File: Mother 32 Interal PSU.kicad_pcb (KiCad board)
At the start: 2 copper layers, 200.7 x 40.6 mm, 24 parts, among them P1 CONN_01X02, P2 CONN_02X08, P3 CONN_02X08, P4 CONN_02X08, P5 CONN_02X08, P6 CONN_02X08, P7 CONN_02X08, P8 CONN_02X08, P9 CONN_02X08, U1 BPM15, U2 R-78E5.0-0.5

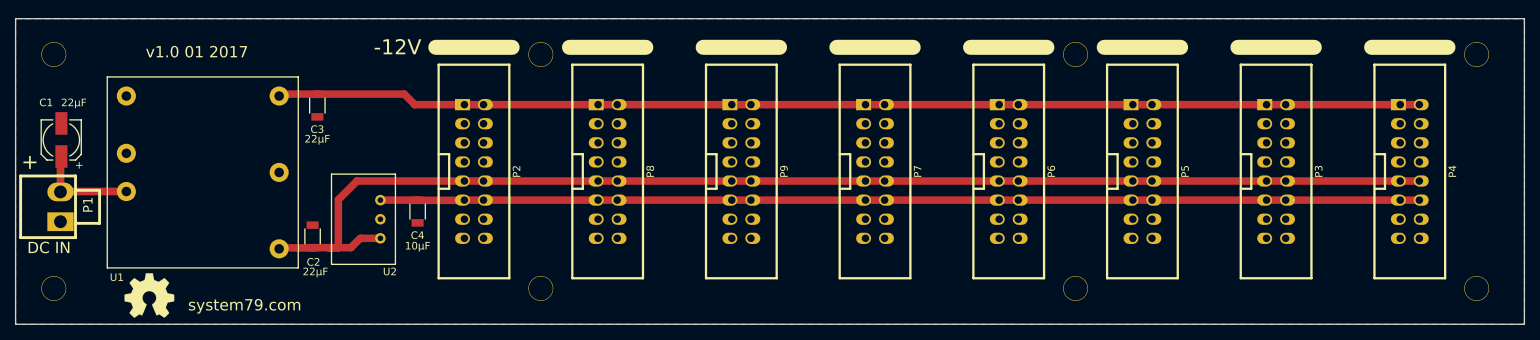
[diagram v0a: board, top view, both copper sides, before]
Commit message: updated silkscreen
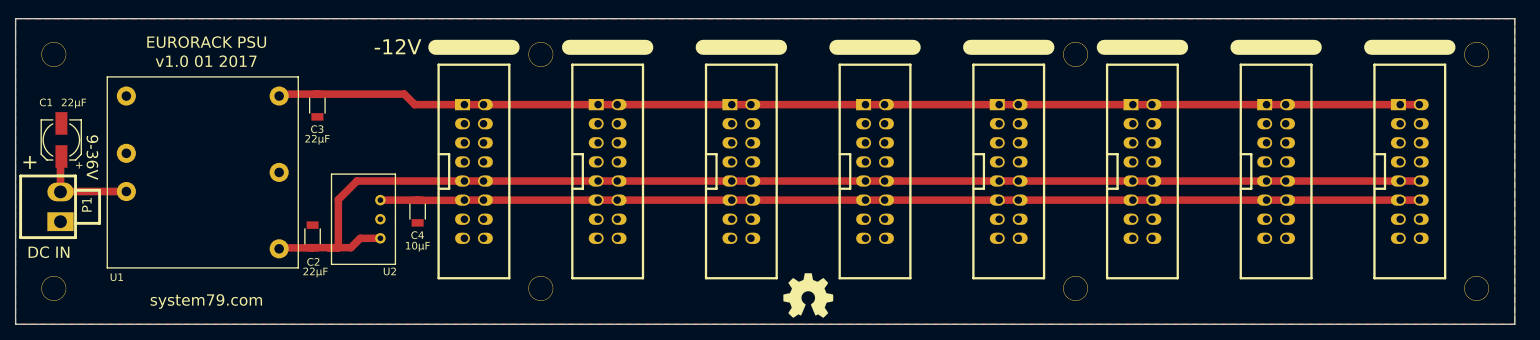
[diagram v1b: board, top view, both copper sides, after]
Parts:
- moved REF*** 87.6 mm to (143.5, 113.0)
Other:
- board size 200.7 x 40.6 mm -> 199.4 x 40.6 mm
- board text added: "9-36V"
- board text added: "EURORACK PSU"
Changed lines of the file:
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@@
     (links 109)
     (no_connects 0)
-    (area 38.024999 76.124999 238.835001 116.915001)
+    (area 38.024999 76.124999 237.565001 116.915001)
     (thickness 1.6)
-    (drawings 17)
+    (drawings 19)
     (tracks 72)
     (zones 0)
@@
     (descr "Box header 8x2pin 2.54mm")
     (tags "CONN DEV")
-    (fp_text reference P9 (at 0 -5.7 270) (layer F.SilkS)
+    (fp_text reference P9 (at 0 -5.7 270) (layer F.SilkS) hide
       (effects (font (size 1 1) (thickness 0.2032)))
     )
@@
     (descr "Box header 8x2pin 2.54mm")
     (tags "CONN DEV")
-    (fp_text reference P8 (at 0 -5.7 270) (layer F.SilkS)
+    (fp_text reference P8 (at 0 -5.7 270) (layer F.SilkS) hide
       (effects (font (size 1 1) (thickness 0.2032)))
     )
@@
     (descr "Box header 8x2pin 2.54mm")
     (tags "CONN DEV")
-    (fp_text reference P7 (at 0 -5.7 270) (layer F.SilkS)
+    (fp_text reference P7 (at 0 -5.7 270) (layer F.SilkS) hide
       (effects (font (size 1 1) (thickness 0.2032)))
     )
@@
     (descr "Box header 8x2pin 2.54mm")
     (tags "CONN DEV")
-    (fp_text reference P6 (at 0 -5.7 270) (layer F.SilkS)
+    (fp_text reference P6 (at 0 -5.7 270) (layer F.SilkS) hide
       (effects (font (size 1 1) (thickness 0.2032)))
     )
@@
     (descr "Box header 8x2pin 2.54mm")
     (tags "CONN DEV")
-    (fp_text reference P5 (at 0 -5.7 270) (layer F.SilkS)
+    (fp_text reference P5 (at 0 -5.7 270) (layer F.SilkS) hide
       (effects (font (size 1 1) (thickness 0.2032)))
     )
@@
     (descr "Box header 8x2pin 2.54mm")
     (tags "CONN DEV")
-    (fp_text reference P4 (at 0 -5.7 270) (layer F.SilkS)
+    (fp_text reference P4 (at 0 -5.7 270) (layer F.SilkS) hide
       (effects (font (size 1 1) (thickness 0.2032)))
     )
@@
     (descr "Box header 8x2pin 2.54mm")
     (tags "CONN DEV")
-    (fp_text reference P3 (at 0 -5.7 270) (layer F.SilkS)
+    (fp_text reference P3 (at 0 -5.7 270) (layer F.SilkS) hide
       (effects (font (size 1 1) (thickness 0.2032)))
     )
@@
     (descr "Box header 8x2pin 2.54mm")
     (tags "CONN DEV")
-    (fp_text reference P2 (at 0 -5.7 270) (layer F.SilkS)
+    (fp_text reference P2 (at 0 -5.7 360) (layer F.SilkS) hide
       (effects (font (size 1 1) (thickness 0.2032)))
     )
@@
     (at 44.069 101.219 270)
     (descr "2 pin vert. connector, Molex KK156 series")
-    (fp_text reference P1 (at -0.254 -3.683 450) (layer F.SilkS)
+    (fp_text reference P1 (at -0.254 -3.556 450) (layer F.SilkS)
       (effects (font (thickness 0.3048)))
     )
@@
   )
   (module Symbols:OSHW-Symbol_6.7x6mm_SilkScreen (layer F.Cu)
-    (at 55.88 113.03)
+    (at 143.51 113.03)
     (descr "Open Source Hardware Symbol")
     (tags "Logo Symbol OSHW")
@@
       (xy 0.555814 -2.531069)) (layer F.SilkS) (width 0.01))
   )
-  (gr_text "v1.0 01 2017" (at 62.23 80.645) (layer F.SilkS)
+  (gr_text 9-36V (at 48.26 94.615 270) (layer F.SilkS)
     (effects (font (size 1.5 1.5) (thickness 0.3)))
   )
-  (gr_text system79.com (at 68.58 114.3) (layer F.SilkS)
+  (gr_text "EURORACK PSU" (at 63.5 79.375) (layer F.SilkS)
     (effects (font (size 1.5 1.5) (thickness 0.3)))
   )
-  (gr_text "DC IN" (at 42.545 106.68) (layer F.SilkS)
+  (gr_text "v1.0 01 2017" (at 63.5 81.915) (layer F.SilkS)
+    (effects (font (size 1.5 1.5) (thickness 0.3)))
+  )
+  (gr_text system79.com (at 63.5 113.665) (layer F.SilkS)
+    (effects (font (size 1.5 1.5) (thickness 0.3)))
+  )
+  (gr_text "DC IN" (at 42.545 107.315) (layer F.SilkS)
     (effects (font (size 1.5 1.5) (thickness 0.3)))
   )
@@
   (gr_line (start 93.98 80.01) (end 104.14 80.01) (angle 90) (layer F.SilkS) (width 2))
   (gr_line (start 38.1 116.84) (end 38.1 76.2) (layer Edge.Cuts) (width 0.15))
-  (gr_line (start 238.76 116.84) (end 38.1 116.84) (layer Edge.Cuts) (width 0.15))
-  (gr_line (start 238.76 76.2) (end 238.76 116.84) (angle 90) (layer Edge.Cuts) (width 0.15))
-  (gr_line (start 38.1 76.2) (end 238.76 76.2) (angle 90) (layer Edge.Cuts) (width 0.15))
+  (gr_line (start 237.49 116.84) (end 38.1 116.84) (layer Edge.Cuts) (width 0.15))
+  (gr_line (start 237.49 76.2) (end 237.49 116.84) (angle 90) (layer Edge.Cuts) (width 0.15))
+  (gr_line (start 38.1 76.2) (end 237.49 76.2) (angle 90) (layer Edge.Cuts) (width 0.15))
   (segment (start 44.069 99.239) (end 44.069 94.656) (width 1) (layer F.Cu) (net 1))
   (segment (start 44.069 94.656) (end 44.196 94.529) (width 1) (layer F.Cu) (net 1))
@@
     (polygon
       (pts
-        (xy 238.76 116.84) (xy 38.1 116.84) (xy 38.1 76.2) (xy 238.76 76.2) (xy 238.76 116.84)
+        (xy 237.49 116.84) (xy 38.1 116.84) (xy 38.1 76.2) (xy 237.49 76.2) (xy 237.49 116.84)
       )
     )

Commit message: updated ground planes and power traces, added CV/GATE connections
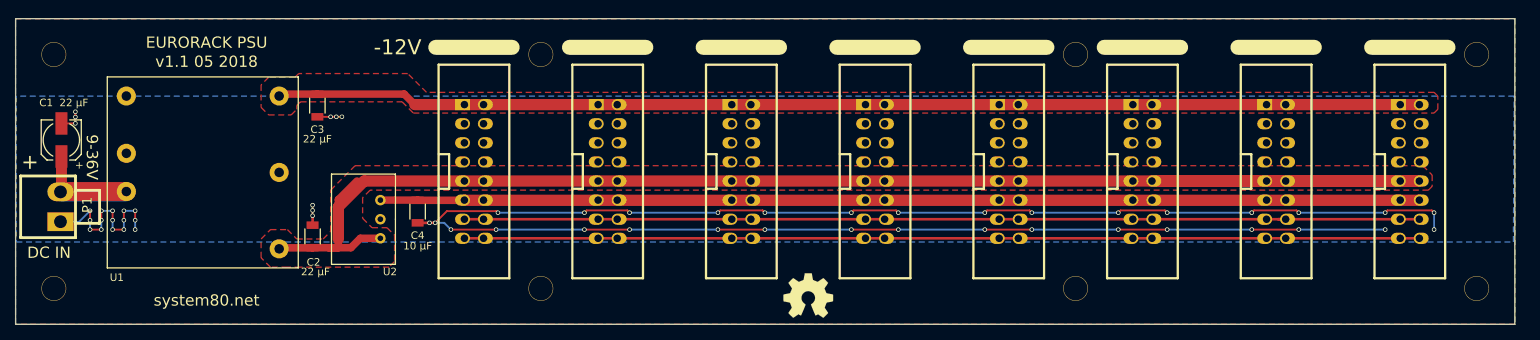
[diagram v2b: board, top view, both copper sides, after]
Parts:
- C1, C2, C3: value 22μF -> 22 μF
- C4: value 10μF -> 10 μF
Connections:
- P2 pad 13: Net-(P2-Pad13) -> /CV
- P2 pad 14: Net-(P2-Pad14) -> /CV
- P2 pad 15: Net-(P2-Pad15) -> /GATE
- P2 pad 16: Net-(P2-Pad16) -> /GATE
- P3 pad 13: Net-(P3-Pad13) -> /CV
- P3 pad 14: Net-(P3-Pad14) -> /CV
- P3 pad 15: Net-(P3-Pad15) -> /GATE
- P3 pad 16: Net-(P3-Pad16) -> /GATE
- P4 pad 13: Net-(P4-Pad13) -> /CV
- P4 pad 14: Net-(P4-Pad14) -> /CV
- P4 pad 15: Net-(P4-Pad15) -> /GATE
- P4 pad 16: Net-(P4-Pad16) -> /GATE
- P5 pad 13: Net-(P5-Pad13) -> /CV
- P5 pad 14: Net-(P5-Pad14) -> /CV
- P5 pad 15: Net-(P5-Pad15) -> /GATE
- P5 pad 16: Net-(P5-Pad16) -> /GATE
- P6 pad 13: Net-(P6-Pad13) -> /CV
- P6 pad 14: Net-(P6-Pad14) -> /CV
- P6 pad 15: Net-(P6-Pad15) -> /GATE
- P6 pad 16: Net-(P6-Pad16) -> /GATE
- P7 pad 13: Net-(P7-Pad13) -> /CV
- P7 pad 14: Net-(P7-Pad14) -> /CV
- P7 pad 15: Net-(P7-Pad15) -> /GATE
- P7 pad 16: Net-(P7-Pad16) -> /GATE
- P8 pad 13: Net-(P8-Pad13) -> /CV
- P8 pad 14: Net-(P8-Pad14) -> /CV
- P8 pad 15: Net-(P8-Pad15) -> /GATE
- P8 pad 16: Net-(P8-Pad16) -> /GATE
- P9 pad 13: Net-(P9-Pad13) -> /CV
- P9 pad 14: Net-(P9-Pad14) -> /CV
- P9 pad 15: Net-(P9-Pad15) -> /GATE
- P9 pad 16: Net-(P9-Pad16) -> /GATE
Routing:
- net GND: track 0.00 -> 299.0 mm, vias 0 -> 57
- net /CV: track 0.00 -> 128.0 mm
- net +5V: track 138.2 -> 265.2 mm
- net -12V: track 152.3 -> 279.3 mm
- net /GATE: track 0.00 -> 127.0 mm
- net +12V: track 166.4 -> 286.3 mm
- net Net-(C1-Pad1): track 13.5 -> 22.3 mm
- added copper zone on F.Cu, net +12V
- added copper zone on F.Cu, net -12V
- added copper zone on B.Cu, net GND
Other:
- rule pad_to_mask_clearance: 0.2 -> 0.01
- board text added: "system80.net"
- board text added: "v1.1 05 2018"
- board text removed: "system79.com"
- board text removed: "v1.0 01 2017"

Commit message: generated gerbers for new version, 1.1
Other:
- rule pad_to_mask_clearance: 0.01 -> 0.05
- board text added: "M32 EURORACK PSU"
- board text removed: "EURORACK PSU"
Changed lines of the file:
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@@
     (pad_size 3.302 3.302)
     (pad_drill 3.175)
-    (pad_to_mask_clearance 0.01)
+    (pad_to_mask_clearance 0.05)
     (aux_axis_origin 0 0)
     (visible_elements 7FFFFF7F)
@@
   (gr_line (start 51.308 86.487) (end 54.356 86.487) (angle 90) (layer Eco1.User) (width 0.2))
   (gr_line (start 52.832 84.963) (end 52.832 88.011) (angle 90) (layer Eco1.User) (width 0.2))
-  (gr_text 9-36V (at 48.26 94.615 270) (layer F.SilkS)
+  (gr_text 9-36V (at 39.75 90.25 270) (layer F.SilkS)
     (effects (font (size 1.5 1.5) (thickness 0.3)))
   )
-  (gr_text "EURORACK PSU" (at 63.5 79.375) (layer F.SilkS)
+  (gr_text "M32 EURORACK PSU" (at 63.5 79.25) (layer F.SilkS)
     (effects (font (size 1.5 1.5) (thickness 0.3)))
   )
-  (gr_text "v1.1 05 2018" (at 63.5 81.915) (layer F.SilkS)
+  (gr_text "v1.1 05 2018" (at 60 81.75) (layer F.SilkS)
     (effects (font (size 1.5 1.5) (thickness 0.3)))
   )

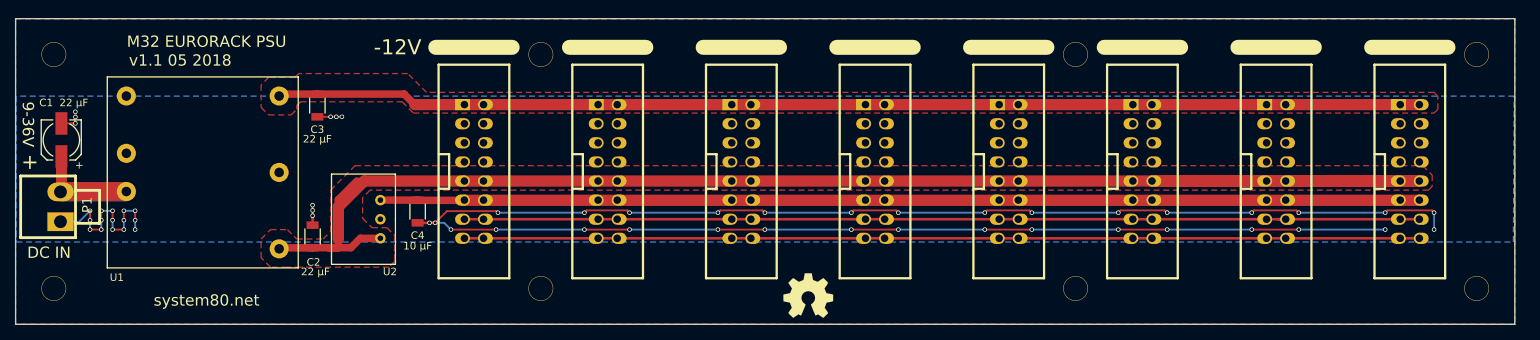
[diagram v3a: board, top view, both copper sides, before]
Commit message: first commit with LDOs but these things will just get too damn hot, so will now revert to just LC filter on output
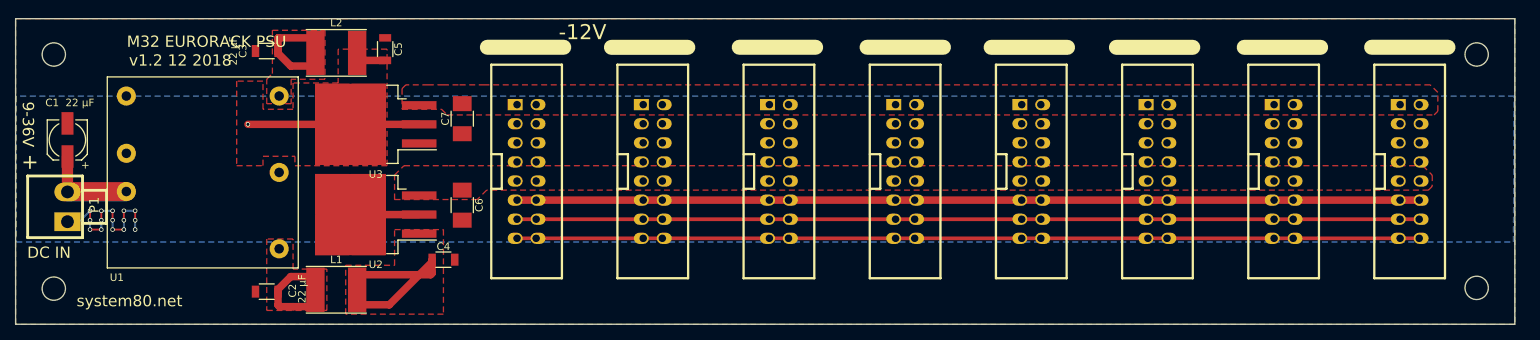
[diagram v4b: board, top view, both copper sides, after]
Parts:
- removed HOLE-0.125-INCH (x8): VAL**, MyModules:HOLE-0.125-INCH
- removed REF***: OSHW-Symbol_6.7x6mm_SilkScreen, Symbols:OSHW-Symbol_6.7x6mm_SilkScreen
- added C5: 10 μF, Capacitors_SMD:C_1206, F.Cu at (87.2, 80.2)
- added C6: 22 μF, Capacitors_SMD:C_1210_HandSoldering, F.Cu at (97.5, 101.0)
- added C7: 22 μF, Capacitors_SMD:C_1210_HandSoldering, F.Cu at (97.5, 89.5)
- added HOLE-M3: VAL**, MyModules:HOLE-M3, F.Cu at (43.2, 81.0)
- added HOLE-M3: VAL**, MyModules:HOLE-M3, F.Cu at (43.2, 112.1)
- added HOLE-M3: VAL**, MyModules:HOLE-M3, F.Cu at (232.4, 112.0)
- added HOLE-M3: VAL**, MyModules:HOLE-M3, F.Cu at (232.4, 81.0)
- added L1: 10 μH, Inductors_SMD:L_Taiyo-Yuden_NR-60xx_HandSoldering, F.Cu at (80.8, 112.2)
- added L2: 10 μH, Inductors_SMD:L_Taiyo-Yuden_NR-60xx_HandSoldering, F.Cu at (80.8, 80.8)
- added U3: LM2990, TO_SOT_Packages_SMD:TO-263-3_TabPin2, F.Cu at (86.0, 90.2)
- U2: value R-78E5.0-0.5 -> LM2940; footprint MyModules:R-78E-0.5 -> TO_SOT_Packages_SMD:TO-263-3_TabPin2
- moved C3 9.90 mm to (71.5, 80.5), turned to 0 degrees
- moved C2 9.55 mm to (71.5, 112.5), turned to 180 degrees
- moved C4 7.26 mm to (95.0, 108.2), turned to 0 degrees
- moved P2 7.00 mm to (106.1, 96.5)
- moved P8 6.00 mm to (122.8, 96.5)
- moved P9 5.00 mm to (139.6, 96.5)
- moved P7 4.00 mm to (156.4, 96.5)
- moved P6 3.00 mm to (173.2, 96.5)
- moved P5 2.00 mm to (190.0, 96.5)
- moved P3 1.00 mm to (206.7, 96.5)
- moved P1 0.93 mm to (45.0, 101.2)
- moved U2 0.87 mm to (86.0, 102.2), turned to 180 degrees
- moved C1 0.80 mm to (45.0, 92.3)
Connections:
- C2 pad 1: +12V -> Net-(C2-Pad1)
- C3 pad 2: -12V -> Net-(C3-Pad2)
- C4 pad 1: +5V -> +V
- U1 pad 4: -12V -> Net-(C3-Pad2)
- U1 pad 6: +12V -> Net-(C2-Pad1)
- U2 pad 1: +12V -> +V
- U2 pad 3: +5V -> +12V
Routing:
- net +12V: track 286.3 -> 0.00 mm
- net -12V: track 279.3 -> 0.00 mm
- net GND: track 299.0 -> 32.2 mm, vias 57 -> 15
- net +5V: track 265.2 -> 120.0 mm
- net -V: track 0.00 -> 29.1 mm, vias 0 -> 1
- net +V: track 0.00 -> 22.0 mm
- net Net-(C3-Pad2): track 0.00 -> 10.7 mm
- net Net-(C2-Pad1): track 0.00 -> 10.6 mm
- net /CV: track 128.0 -> 120.0 mm
- net /GATE: track 127.0 -> 120.0 mm
- net Net-(C1-Pad1): track 22.3 -> 20.5 mm
- added copper zone on F.Cu, net +V
- added copper zone on F.Cu, net -V
- added copper zone on F.Cu, net Net-(C2-Pad1)
- added copper zone on F.Cu, net Net-(C3-Pad2)
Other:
- board text added: "v1.2 12 2018"
- board text removed: "v1.1 05 2018"

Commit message: added LC filter to outputs
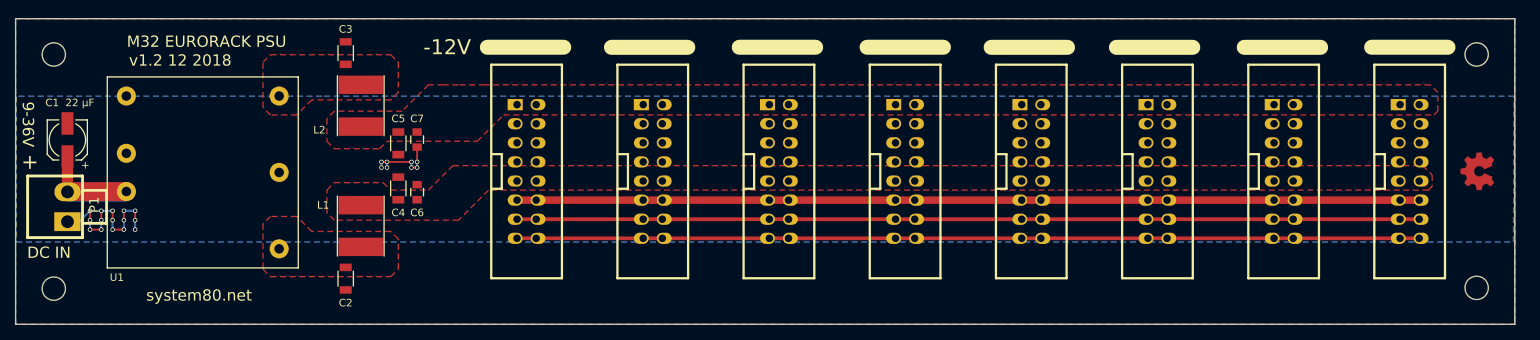
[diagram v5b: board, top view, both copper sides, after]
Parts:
- removed U2: LM2940, TO_SOT_Packages_SMD:TO-263-3_TabPin2
- removed U3: LM2990, TO_SOT_Packages_SMD:TO-263-3_TabPin2
- added G***: LOGO, Logo_copper_OSHW_6x6mm, F.Cu at (232.5, 96.5)
- C6, C7: value 22 μF -> 1 μF; footprint Capacitors_SMD:C_1210_HandSoldering -> Capacitors_SMD:C_0805
- moved C5 12.6 mm to (89.0, 92.8), turned to 90 degrees
- moved C4 11.2 mm to (89.0, 98.8), turned to 90 degrees
- moved C2 10.6 mm to (82.0, 110.8), turned to 270 degrees
- moved C3 10.5 mm to (82.0, 80.8), turned to 270 degrees
- moved L1 9.08 mm to (84.0, 103.8), turned to 90 degrees
- moved L2 7.74 mm to (84.0, 87.8), turned to 270 degrees
- moved C7 6.61 mm to (91.5, 92.3)
- moved C6 6.24 mm to (91.5, 99.3), turned to 90 degrees
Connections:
- C4 pad 1: +V -> +12V
- C5 pad 2: -V -> -12V
- L1 pad 2: +V -> +12V
- L2 pad 2: -V -> -12V
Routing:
- net -V: track 29.1 -> 0.00 mm, vias 1 -> 0
- net +V: track 22.0 -> 0.00 mm
- net Net-(C2-Pad1): track 10.6 -> 0.18 mm
- net Net-(C3-Pad2): track 10.7 -> 0.43 mm
- net GND: track 32.2 -> 32.8 mm, vias 15 -> 23
- removed copper zone on F.Cu, net +V
- removed copper zone on F.Cu, net -V

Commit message: 4 layer
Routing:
- added copper zone on In2.Cu, net +12V
- added copper zone on In2.Cu, net -12V
- added copper zone on In1.Cu, net GND
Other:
- copper layers 2 -> 4
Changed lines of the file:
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@@
     (links 144)
     (no_connects 0)
-    (area 38.024999 76.124999 237.565001 116.915001)
+    (area 36.276 74.485 238.042144 118.425)
     (thickness 1.6)
     (drawings 47)
@@
   (layers
     (0 F.Cu signal)
+    (1 In1.Cu signal)
+    (2 In2.Cu signal)
     (31 B.Cu signal)
     (32 B.Adhes user)
@@
     (47 F.CrtYd user)
     (48 B.Fab user)
-    (49 F.Fab user hide)
+    (49 F.Fab user)
   )
   (setup
@@
       )
     )
+  )
+  (zone (net 2) (net_name GND) (layer In1.Cu) (hatch edge 0.508)
+    (connect_pads (clearance 0.3))
+    (min_thickness 0.254)
+    (fill yes (arc_segments 16) (thermal_gap 0.508) (thermal_bridge_width 1))
+    (polygon
+      (pts
+        (xy 38.1 76.2) (xy 237.5 76.2) (xy 237.5 116.8) (xy 38.1 116.8)
+      )
+    )
+  )
+  (zone (net 4) (net_name -12V) (layer In2.Cu) (hatch edge 0.508)
+    (priority 1)
+    (connect_pads (clearance 0.3))
+    (min_thickness 0.254)
+    (fill yes (arc_segments 16) (thermal_gap 0.508) (thermal_bridge_width 1.5))
+    (polygon
+      (pts
+        (xy 86.5 93.5) (xy 87.5 92.5) (xy 99.5 92.5) (xy 103 89) (xy 226.75 89)
+        (xy 227.25 88.5) (xy 227.25 86) (xy 226.25 85) (xy 100.5 85) (xy 97 85)
+        (xy 95 85) (xy 93 85) (xy 89.5 88.5) (xy 80.5 88.5) (xy 79.5 89.5)
+        (xy 79.5 92.5) (xy 80.5 93.5)
+      )
+    )
+  )
+  (zone (net 3) (net_name +12V) (layer In2.Cu) (hatch edge 0.508)
+    (priority 1)
+    (connect_pads (clearance 0.3))
+    (min_thickness 0.254)
+    (fill yes (arc_segments 16) (thermal_gap 0.508) (thermal_bridge_width 1.5))
+    (polygon
+      (pts
+        (xy 96.25 95.75) (xy 225.25 95.75) (xy 226.5 97) (xy 226.5 98.5) (xy 226 99)
+        (xy 101 99) (xy 97 103) (xy 80.5 103) (xy 79.5 102) (xy 79.5 99)
+        (xy 80.5 98) (xy 87 98) (xy 88 99) (xy 93 99)
+      )
+    )
